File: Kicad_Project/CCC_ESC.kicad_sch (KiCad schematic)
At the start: 228 parts, among them J1 Conn_01x07, J2 Conn_01x06, J3 Conn_01x06, J4 Conn_01x06, SW1 Conn_01x02, U1 NCP5183 / TF2190-TAH, U2 NCP5183 / TF2190-TAH, U3 NCP5183 / TF2190-TAH, U4 NCS20034DR2G, U5 STM32F401CCU6_Balckpill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

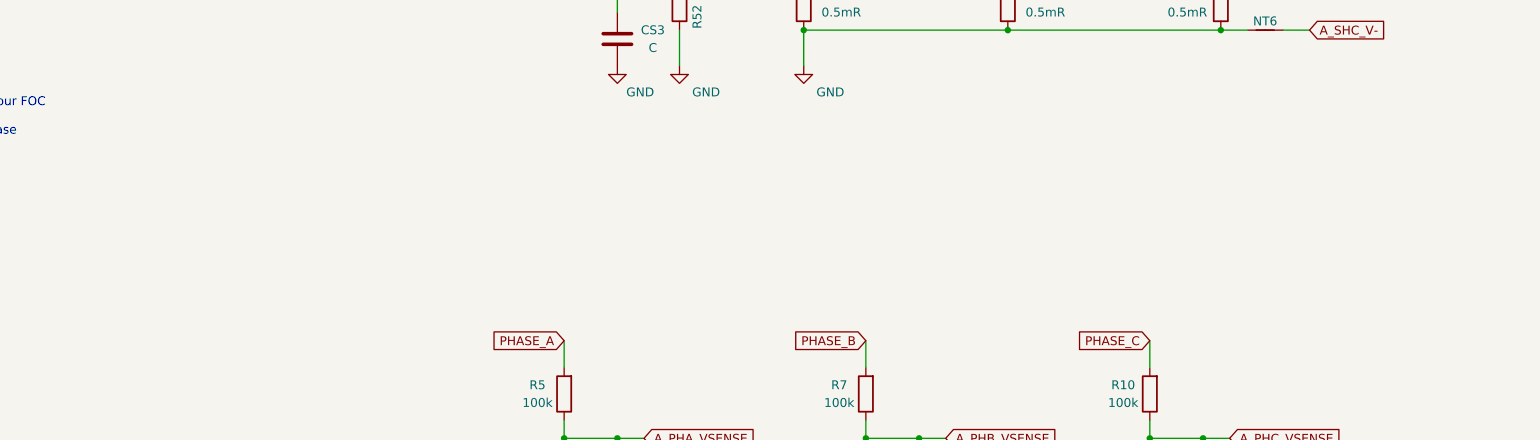
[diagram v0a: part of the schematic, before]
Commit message: fixed most of DMs suggestions
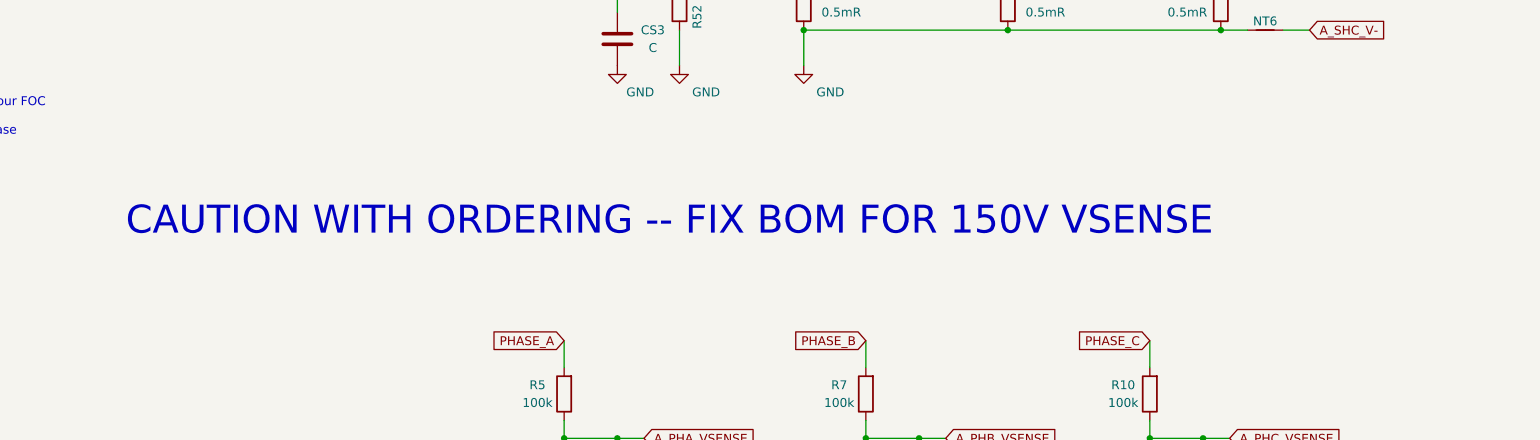
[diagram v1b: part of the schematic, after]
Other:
- note added: "CAUTION WITH ORDERING -- FIX BOM FOR 150V VSENSE"
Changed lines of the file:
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@@
     (effects (font (size 1.27 1.27)) (justify left bottom))
+  )
+  (text "CAUTION WITH ORDERING -- FIX BOM FOR 150V VSENSE" (at 377.952 300.228 0)
+    (effects (font (size 4 4)) (justify left bottom))
   )
   (text "--> Protect logic board" (at 175.768 122.682 0)
